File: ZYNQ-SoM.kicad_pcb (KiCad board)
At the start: 6 copper layers, 50 x 40 mm, 136 parts, among them J401 AXK500137YG, J402 AXK500137YG, U201 xc7z010clg400, U202 W25Q256FVEI, U301 MT41K256M16TW-107_P, U501 TPS62130ARGTR, U502 TPS62130ARGTR, U503 SPX3819M5-L-3-3, U504 TPS62130ARGTR, U701 33.3333MHz

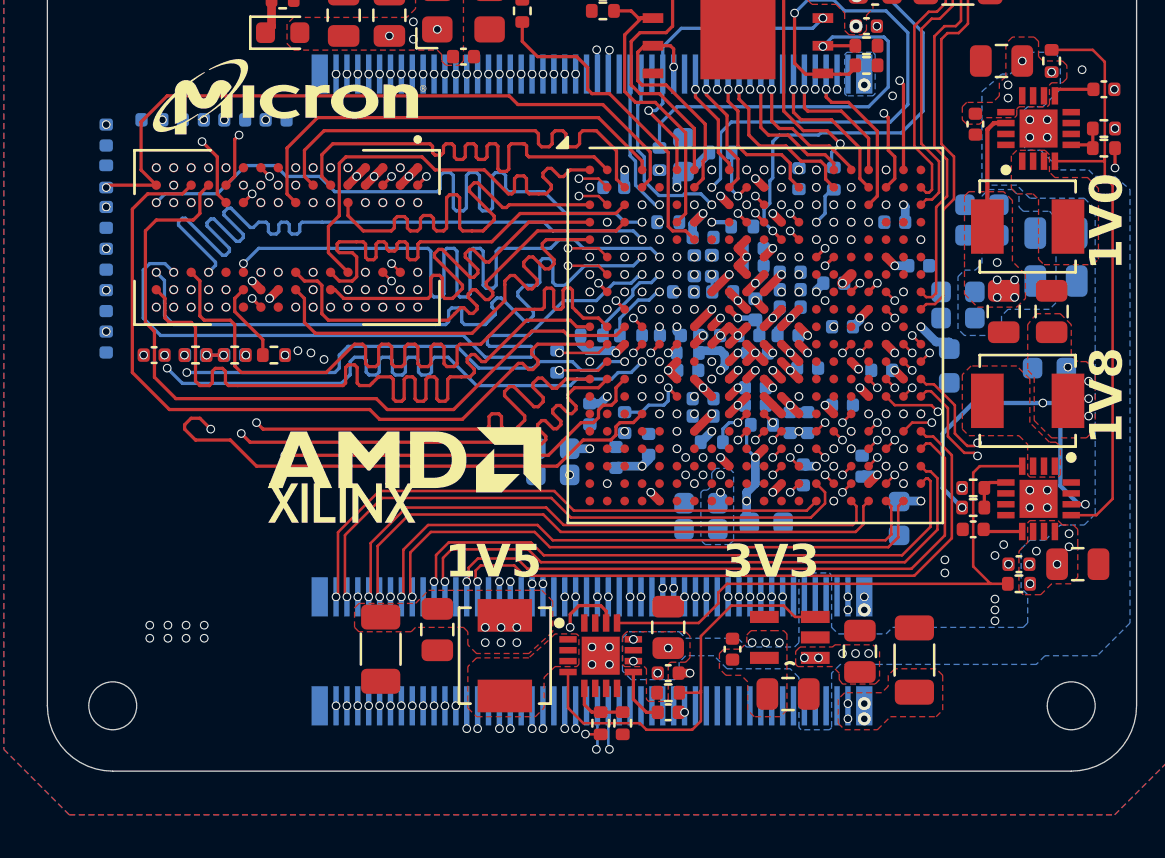
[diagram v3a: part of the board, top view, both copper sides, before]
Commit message: layout: add bank 34 pl pair
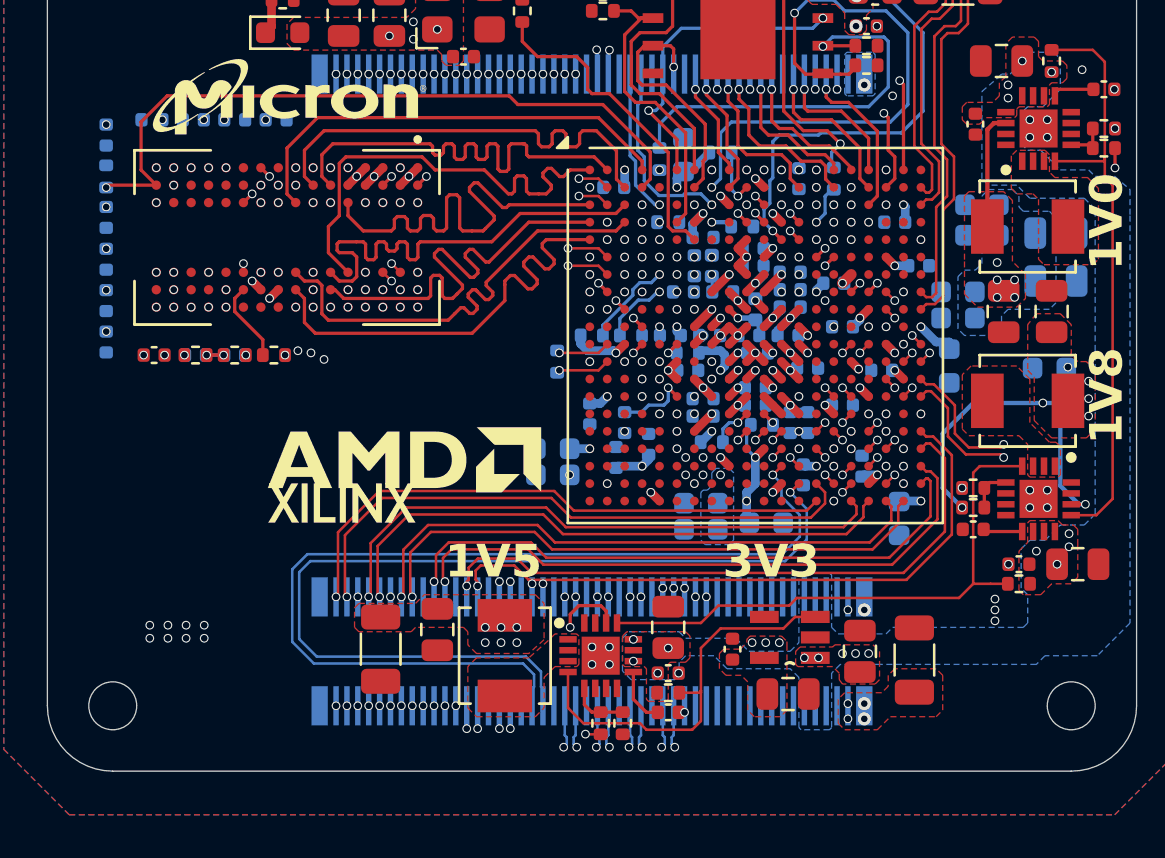
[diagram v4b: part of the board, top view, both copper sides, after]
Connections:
- J401 pad 13: unconnected-(J401-Pad13) -> +5V
- J401 pad 14: unconnected-(J401-Pad14) -> +5V
- J401 pad 15: GND -> +5V
- J401 pad 16: GND -> +5V
- J401 pad 18: PL_B34_IO22_P -> unconnected-(J401-Pad18)
- J401 pad 20: PL_B34_IO22_N -> unconnected-(J401-Pad20)
- J401 pad 24: PL_B34_IO12_N -> unconnected-(J401-Pad24)
- J401 pad 26: PL_B34_IO12_P -> unconnected-(J401-Pad26)
- J401 pad 30: PL_B34_IO20_P -> unconnected-(J401-Pad30)
- J401 pad 32: PL_B34_IO20_N -> unconnected-(J401-Pad32)
- J401 pad 35: unconnected-(J401-Pad35) -> PL_B34_IO14_N
- J401 pad 36: PL_B34_IO13_P -> PL_B34_IO22_P
- J401 pad 37: unconnected-(J401-Pad37) -> PL_B34_IO14_P
- J401 pad 38: PL_B34_IO13_N -> PL_B34_IO22_N
- J401 pad 41: unconnected-(J401-Pad41) -> PL_B34_IO13_P
- J401 pad 43: unconnected-(J401-Pad43) -> PL_B34_IO13_N
- J401 pad 47: PL_B34_IO23_N -> PL_B34_IO24_N
- J401 pad 49: PL_B34_IO25 -> PL_B34_IO24_P
- J401 pad 53: PL_B34_IO0 -> PL_B34_IO20_N
- J401 pad 55: PL_B34_IO23_P -> PL_B34_IO20_P
- J401 pad 59: PL_B34_IO4_P -> PL_B34_IO4_N
- J401 pad 61: PL_B34_IO4_N -> PL_B34_IO4_P
- J401 pad 65: PL_B34_IO14_P -> PL_B34_IO12_P
- J401 pad 67: PL_B34_IO14_N -> PL_B34_IO12_N
- U201 pad P15: unconnected-(U201C-IO_L24P_T3_34-PadP15) -> PL_B34_IO24_P
- U201 pad P16: unconnected-(U201C-IO_L24N_T3_34-PadP16) -> PL_B34_IO24_N
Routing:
- net PL_B34_IO23_P: track 42.2 -> 0.00 mm, vias 2 -> 0
- net PL_B34_IO24_P: track 0.00 -> 38.5 mm, vias 0 -> 2
- net PL_B34_IO24_N: track 0.00 -> 38.3 mm, vias 0 -> 2
- net /DDR3/DDR_A3: track 35.1 -> 0.00 mm
- net /DDR3/DDR_A1: track 35.0 -> 0.00 mm
- net /DDR3/DDR_A8: track 35.0 -> 0.00 mm
- net /DDR3/DDR_A5: track 35.0 -> 0.00 mm
- net /DDR3/DDR_A11: track 33.7 -> 0.09 mm
- net /DDR3/DDR_A12: track 33.6 -> 0.07 mm
- net /DDR3/DDR_~{CS}: track 33.4 -> 0.00 mm, vias 2 -> 0
- net /DDR3/DDR_BA0: track 33.3 -> 0.00 mm, vias 2 -> 0
- net /DDR3/DDR_A0: track 33.3 -> 0.00 mm, vias 2 -> 0
- net /DDR3/DDR_BA1: track 33.3 -> 0.00 mm, vias 2 -> 0
- net /DDR3/DDR_BA2: track 33.3 -> 0.00 mm, vias 2 -> 0
- net /DDR3/DDR_~{CAS}: track 33.3 -> 0.00 mm
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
